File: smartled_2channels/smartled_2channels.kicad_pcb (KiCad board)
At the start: 2 copper layers, 76 parts, among them J1 Conn_01x04, J2 Conn_01x02, SW1 SW_Push, U1 OC5028B, U2 MAX485E, U3 PY32F003F1xUx, U4 OC5864, U5 SGM2033-3.3, U6 OC5028B, U7 GS8521

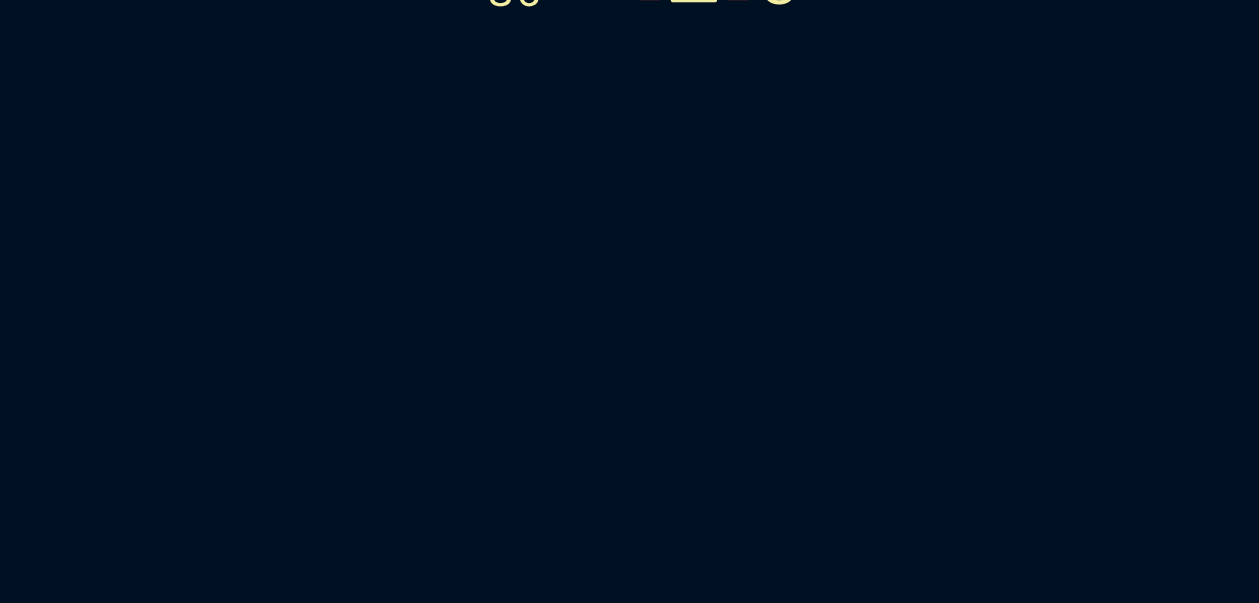
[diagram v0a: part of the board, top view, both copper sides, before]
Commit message: 添加麦克风声感应电路，红外和雷达传感器接口
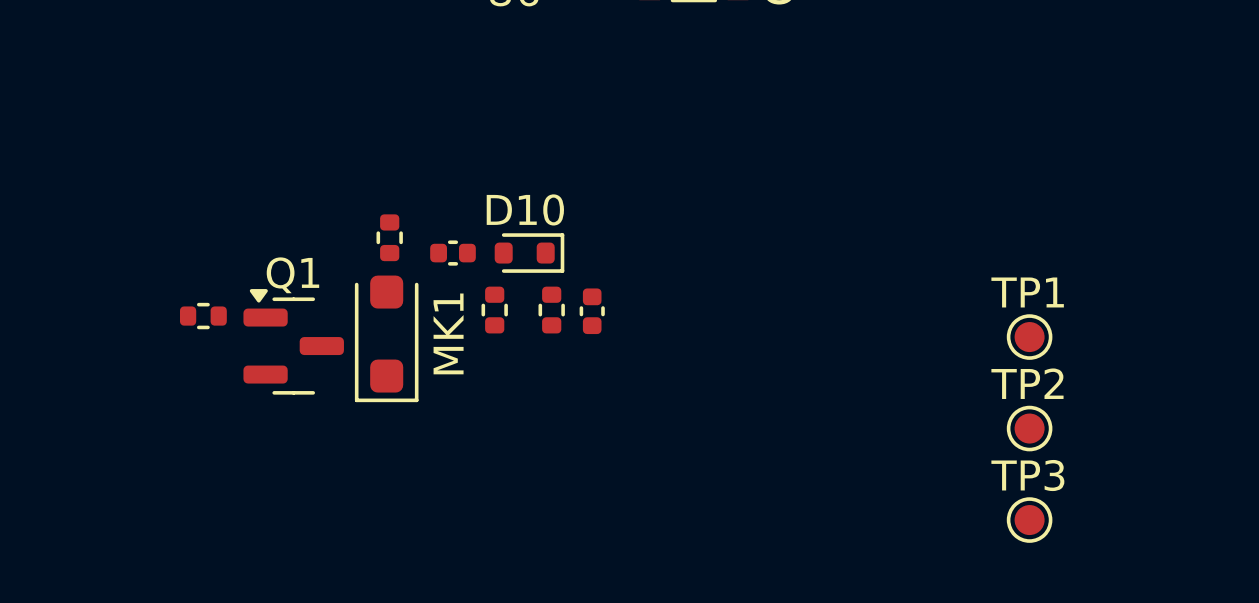
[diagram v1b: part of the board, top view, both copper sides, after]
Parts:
- added C10: 100n, Capacitor_SMD:C_0402_1005Metric, F.Cu at (157.7, 111.1)
- added C14: 100n, Capacitor_SMD:C_0402_1005Metric, F.Cu at (162.3, 113.0)
- added D10: D, Diode_SMD:D_SOD-523, F.Cu at (160.1, 111.1)
- added MK1: Microphone, Diode_SMD:D_SOD-123F, F.Cu at (155.5, 113.8)
- added Q1: Q_NMOS_GSD, Package_TO_SOT_SMD:SOT-23, F.Cu at (152.4, 114.2)
- added R21: 47k, Resistor_SMD:R_0402_1005Metric, F.Cu at (155.6, 110.6)
- added R22: 100k, Resistor_SMD:R_0402_1005Metric, F.Cu at (159.1, 113.0)
- added R24: 200k, Resistor_SMD:R_0402_1005Metric, F.Cu at (161.0, 113.0)
- added R25: 1k, Resistor_SMD:R_0402_1005Metric, F.Cu at (149.4, 113.2)
- added TP1: TestPoint, TestPoint:TestPoint_Pad_D1.0mm, F.Cu at (176.9, 113.9)
- added TP2: TestPoint, TestPoint:TestPoint_Pad_D1.0mm, F.Cu at (176.9, 117.0)
- added TP3: TestPoint, TestPoint:TestPoint_Pad_D1.0mm, F.Cu at (176.9, 120.0)
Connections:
- U3 pad 13: unconnected-(U3-OSCIN_PF0-Pad13) -> /INT_RADAR
- U3 pad 14: unconnected-(U3-OSCOUT_PF1-Pad14) -> /INT_IR
- U3 pad 15: unconnected-(U3-NRST_PF2-Pad15) -> /DET_EN
- U3 pad 17: /PWM4 -> /ADC_RADAR
- U3 pad 19: /PWM3 -> /ADC_MIC

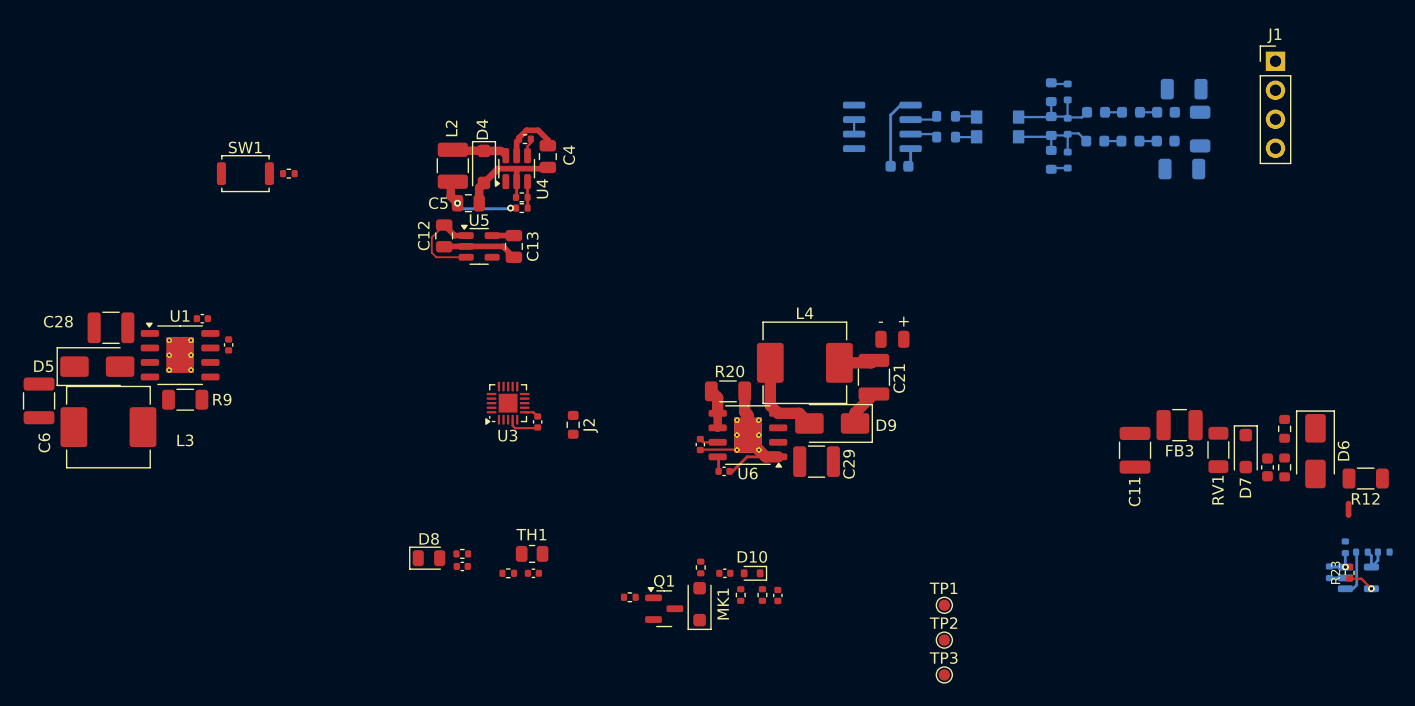
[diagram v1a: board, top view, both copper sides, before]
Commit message: 压缩布局至85.4x16mm尺寸
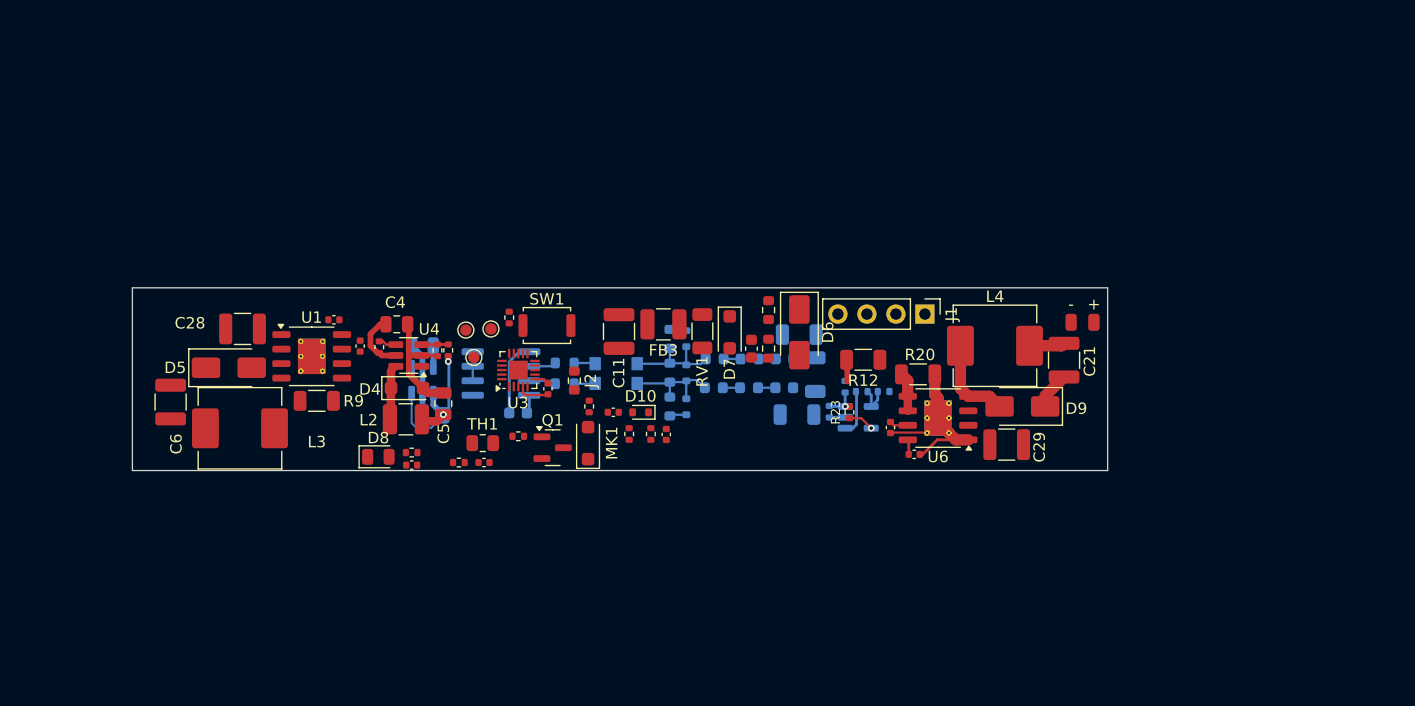
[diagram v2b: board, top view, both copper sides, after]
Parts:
- C12, C13, U5: moved to B.Cu
- moved TP3 51.6 mm to (135.0, 89.8), turned to 90 degrees
- moved TP2 48.2 mm to (137.2, 89.7), turned to 90 degrees
- moved TP1 46.6 mm to (135.7, 92.2), turned to 90 degrees
- moved C11 46.4 mm to (148.4, 89.9)
- moved C9 46.4 mm to (160.0, 91.4)
- moved D6 46.4 mm to (164.2, 90.0)
- moved D7 46.4 mm to (158.1, 90.0)
- moved R10 46.4 mm to (161.5, 88.0)
- moved R11 46.4 mm to (161.5, 91.4)
- moved RV1 46.4 mm to (155.7, 89.9)
- moved FB3 46.1 mm to (152.3, 89.3)
- moved R18 46.0 mm to (169.7, 95.2)
- moved R23 46.0 mm to (168.6, 97.0)
- moved R16 46.0 mm to (168.2, 94.8)
- moved R17 46.0 mm to (171.6, 95.2)
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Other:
- board outline added: 85.4 x 16 mm

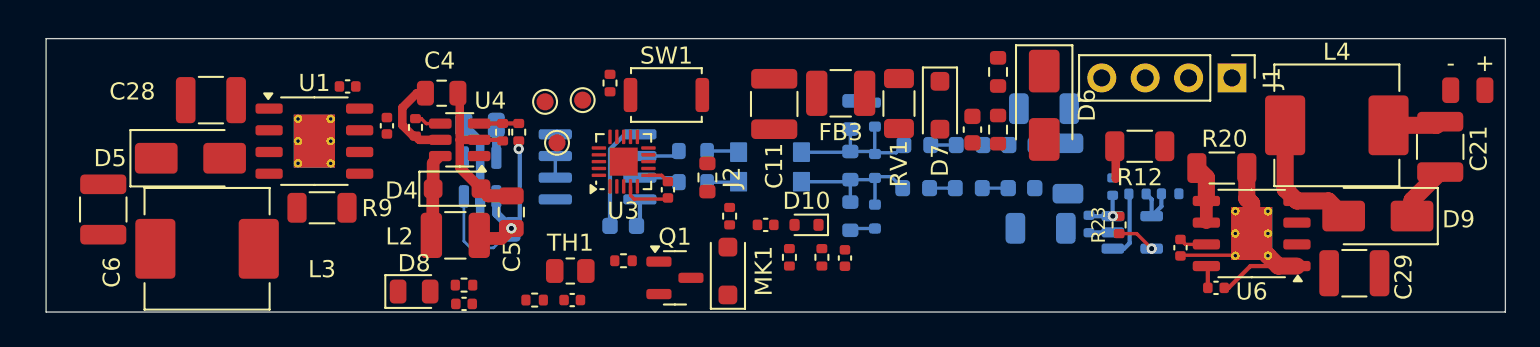
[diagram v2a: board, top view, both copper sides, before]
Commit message: 进行布线，微调原理图
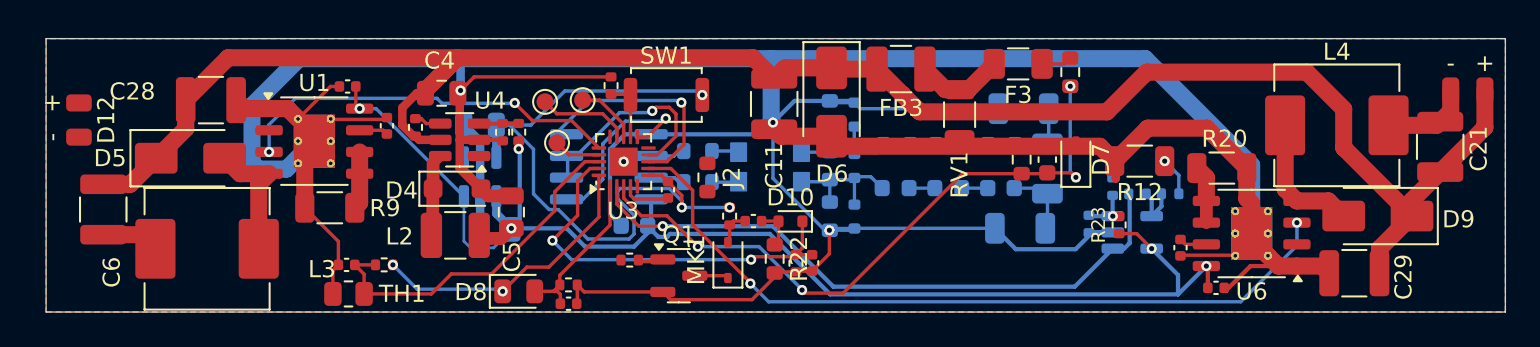
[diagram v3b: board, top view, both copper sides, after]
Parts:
- removed J1: Conn_01x04, Connector_PinHeader_2.54mm:PinHeader_1x04_P2.54mm_Vertical
- added D12: LED_Series, project_footprints:2Pads_1.0x1.5mm_P2.0mm_mpsign, F.Cu at (107.7, 90.9)
- added F3: Fuse, Fuse:Fuse_1206_3216Metric, F.Cu at (162.7, 87.6)
- D7, MK1: footprint Diode_SMD:D_SOD-123F -> Diode_SMD:D_SOD-323
- R22: footprint Resistor_SMD:R_0402_1005Metric -> Resistor_SMD:R_0603_1608Metric
- moved C17 13.4 mm to (123.4, 99.3), turned to 180 degrees
- moved TH1 13.0 mm to (123.5, 101.0), turned to 180 degrees
- moved D6 12.4 mm to (151.8, 89.8)
- moved R15 9.04 mm to (125.6, 99.3), turned to 180 degrees
- moved D7 8.56 mm to (166.1, 93.2), turned to 90 degrees
- moved C18 6.12 mm to (136.4, 101.6)
- moved D8 6.12 mm to (133.5, 100.9)
- moved R14 6.12 mm to (136.4, 100.5)
- moved C9 4.72 mm to (164.4, 93.2), turned to 90 degrees
- moved R10 4.23 mm to (165.7, 88.1)
- moved FB3 3.80 mm to (155.8, 87.9)
- moved RV1 3.61 mm to (159.3, 90.6)
- moved R11 2.23 mm to (162.9, 93.2), turned to 90 degrees
- moved C14 1.94 mm to (150.6, 99.2)
- moved R24 1.56 mm to (149.7, 99.2)
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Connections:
- R23 pad 1: +3.3V -> +5V
- U7 pad 5: +3.3V -> +5V
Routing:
- net GND: track 49.6 -> 258.4 mm, vias 0 -> 4
- net VINP: track 8.56 -> 109.7 mm
- net +5V: track 18.8 -> 78.2 mm, vias 2 -> 5
- net /PWM2: track 0.00 -> 45.1 mm, vias 0 -> 2
- net /ADC_V: track 0.00 -> 38.0 mm, vias 0 -> 4
- net +3.3V: track 5.47 -> 40.7 mm, vias 1 -> 3
- net /ADC_I: track 4.02 -> 37.0 mm, vias 0 -> 1
- net /ADC_MIC: track 0.00 -> 23.5 mm, vias 0 -> 2
- net /PWM1: track 0.00 -> 22.8 mm, vias 0 -> 2
- net /ADC_T: track 0.00 -> 20.7 mm
- net /SampEn: track 0.00 -> 16.9 mm, vias 0 -> 2
- net /MAX485_DI: track 0.00 -> 13.3 mm, vias 0 -> 1
- net /MAX485_RO: track 0.00 -> 11.7 mm, vias 0 -> 1
- net /MAX485_TR: track 1.27 -> 12.3 mm, vias 0 -> 1
- net /ADC_PD: track 0.00 -> 9.51 mm
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- added copper zone on B.Cu, net GND
- added copper zone on F.Cu, net GND

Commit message: 连接一些未连接项目
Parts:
- moved TP3 0.46 mm to (135.2, 89.4)
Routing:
- net /DET_EN: track 0.00 -> 15.5 mm, vias 0 -> 2
- net /ADC_MIC: track 23.5 -> 25.6 mm
- net GND: track 258.4 -> 260.0 mm, vias 4 -> 5
- net +5V: track 78.2 -> 78.9 mm
- net +3.3V: track 40.7 -> 41.3 mm

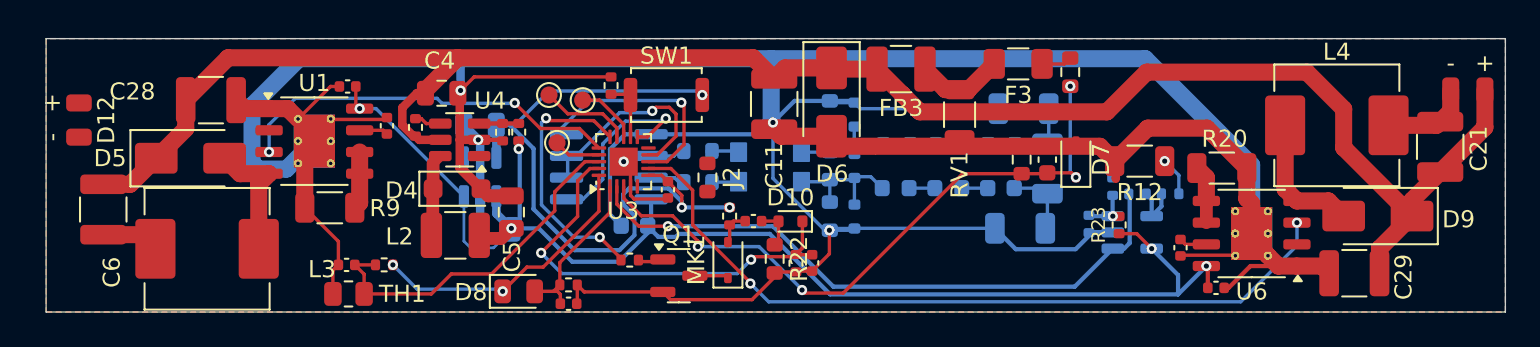
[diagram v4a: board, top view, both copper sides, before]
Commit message: 修改LED输出焊盘，缩短PCB长度到83mm
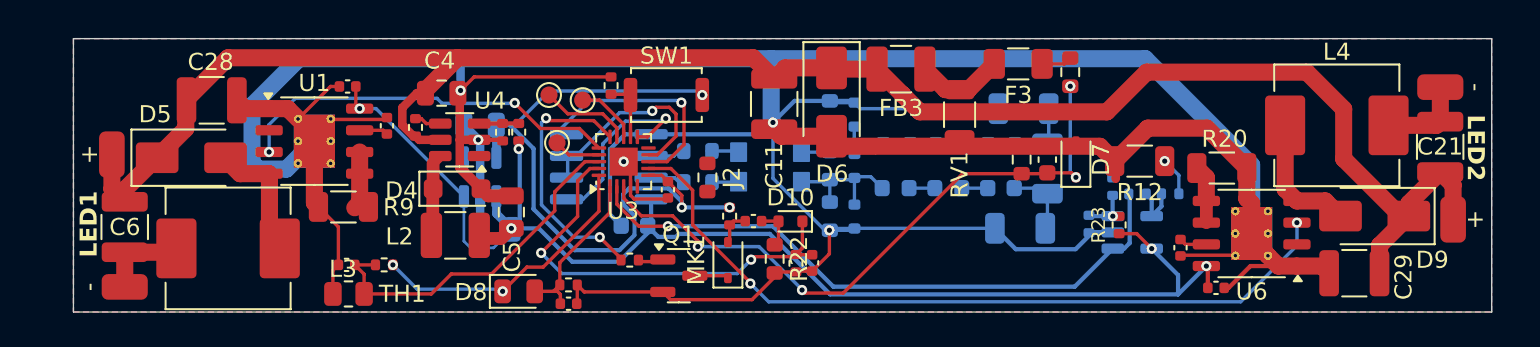
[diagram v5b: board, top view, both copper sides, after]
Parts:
- D12, D13: footprint project_footprints:2Pads_1.0x1.5mm_P2.0mm_mpsign -> project_footprints:2Pads_1.5x2.7mm_Tshape_mpsign
- moved D12 6.81 mm to (110.4, 97.1)
- moved D13 3.69 mm to (187.4, 92.4), turned to -90 degrees
- moved C6 1.62 mm to (110.4, 97.1)
- moved L3 1.23 mm to (116.5, 98.4)
- moved R9 0.80 mm to (123.2, 96.0)
- moved D9 0.19 mm to (183.6, 96.5)
- moved D5 0.06 mm to (114.3, 93.1)
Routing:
- net Net-(D12-K): track 3.39 -> 5.15 mm
- net GND: track 260.0 -> 259.5 mm
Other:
- board size 85.4 x 16 mm -> 83 x 16 mm
- board text added: "LED1"
- board text added: "LED2"

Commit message: 修改丝印
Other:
- board text added: "LED Strip 2 Channel Driver yyyy.mm.dd vx.x-gxxxxxxx Copyright (C) 2026 徐瑞骏 License under CERN-OHL-S v2"
- board text added: "https://github.com/XuHg-zjcn/smartled_controll"
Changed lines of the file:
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@@
 		(tags "Diode SOD523")
 		(property "Reference" "D10"
-			(at 0 1.4 0)
+			(at -2.8496 -0.0058 0)
 			(layer "F.SilkS")
 			(effects
@@
 		(tags "resistor")
 		(property "Reference" "R9"
-			(at -3.2325 -0.025 0)
+			(at -0.33 -1.77 0)
 			(layer "F.SilkS")
 			(effects
@@
 		(tags "SOD-323")
 		(property "Reference" "MK1"
-			(at 0 -1.85 90)
+			(at -2.4 0.71 180)
 			(layer "F.SilkS")
 			(effects
@@
 		(tags "SOD-323")
 		(property "Reference" "D7"
-			(at 0 1.4732 90)
+			(at 1.9272 0.0548 180)
 			(layer "F.SilkS")
 			(effects
@@
 		(tags "resistor")
 		(property "Reference" "R22"
-			(at 0 -1.43 -90)
+			(at 2.2298 0.0076 0)
 			(layer "F.SilkS")
+			(hide yes)
 			(effects
 				(font
@@
 		(tags "Inductor molded power shielded")
 		(property "Reference" "L3"
-			(at -6.725 -1.2 0)
+			(at -4.87 -0.135 -90)
 			(layer "F.SilkS")
 			(effects
@@
 		(tags "capacitor")
 		(property "Reference" "C2"
-			(at -0.005 1.34 0)
+			(at -2.05 2.55 0)
 			(layer "B.SilkS")
 			(effects
@@
 		(tags "capacitor")
 		(property "Reference" "C1"
-			(at 0.075 -1.4 0)
+			(at -1.96 -2.83 0)
 			(layer "B.SilkS")
 			(effects
@@
 			(at -0.01 1.26 90)
 			(layer "B.SilkS")
+			(hide yes)
 			(effects
 				(font
@@
 		(layer "Edge.Cuts")
 	)
+	(gr_text "https://github.com/XuHg-zjcn/smartled_controll"
+		(at 139.49 100.9 0)
+		(layer "B.SilkS")
+		(effects
+			(font
+				(size 0.8 0.8)
+				(thickness 0.1)
+			)
+			(justify left bottom mirror)
+		)
+	)
+	(gr_text "LED Strip 2 Channel Driver\nyyyy.mm.dd vx.x-gxxxxxxx\n\nCopyright (C) 2026  徐瑞骏\nLicense under CERN-OHL-S v2"
+		(at 128.54 97.11 0)
+		(layer "B.SilkS")
+		(effects
+			(font
+				(size 0.8 0.8)
+				(thickness 0.1)
+			)
+			(justify left bottom mirror)
+		)
+	)
 	(gr_text "LED1"
 		(at 108.88 98.91 90)
@@
 	)
 	(segment
-		(start 124.15 95.7125)
-		(end 123.8625 96)
+		(start 124.15 95.4375)
+		(end 124.6625 95.95)
 		(width 1)
 		(layer "F.Cu")
@@
 	(segment
 		(start 124.15 92.735)
-		(end 124.15 95.7125)
+		(end 124.15 95.4375)
 		(width 1)
 		(layer "F.Cu")
@@
 	)
 	(group "LED驱动1"
-		(members "097316fb-18b5-480e-862f-6f3a3067adb6" "178e6880-8828-4553-bee4-e2de0b5de154"
-			"17a861f3-fc8d-4d16-9c42-8d2c828430de" "1b08897a-7ea3-4d59-91b4-9b10cab0b1a9"
-			"2033e229-ce9b-4350-acb4-26b53c010734" "20926de3-6061-49c6-a51c-7a7e43ec4d50"
-			"2152c6b9-174d-424b-a63c-def9bc6348bc" "2a837293-223a-42a8-b839-e46fae8bb605"
-			"2c3bac7e-ebed-4ce1-8919-bbaeaaef3147" "2dabf7f8-eef8-4994-8a27-e8a169fa6792"
-			"2e25fb8c-2a1e-4550-b22c-549ad53cfbc1" "32ae1743-d038-41f1-94bd-7f9fbec4ed90"
-			"37747a8a-c22f-403b-aec3-d528845dcaa8" "479d0d2b-0dce-436a-b1ad-8536b169c966"
-			"48e1d37f-9f97-467d-ba60-32f792c0eb09" "4bd7aa62-10d7-493a-9aaa-15b3a4a61b62"
-			"4c631bd3-adb7-4b47-ab74-286c30ad1970" "50ea2e16-1790-43fd-bae8-e2b482237c03"
+		(members "097316fb-18b5-480e-862f-6f3a3067adb6" "148c36cd-57e3-43ec-9491-cfc7f3f19676"
+			"178e6880-8828-4553-bee4-e2de0b5de154" "17a861f3-fc8d-4d16-9c42-8d2c828430de"
+			"1b08897a-7ea3-4d59-91b4-9b10cab0b1a9" "2033e229-ce9b-4350-acb4-26b53c010734"
+			"20926de3-6061-49c6-a51c-7a7e43ec4d50" "2152c6b9-174d-424b-a63c-def9bc6348bc"
+			"2a837293-223a-42a8-b839-e46fae8bb605" "2c3bac7e-ebed-4ce1-8919-bbaeaaef3147"
+			"2dabf7f8-eef8-4994-8a27-e8a169fa6792" "2e25fb8c-2a1e-4550-b22c-549ad53cfbc1"
+			"32ae1743-d038-41f1-94bd-7f9fbec4ed90" "37747a8a-c22f-403b-aec3-d528845dcaa8"
+			"479d0d2b-0dce-436a-b1ad-8536b169c966" "48e1d37f-9f97-467d-ba60-32f792c0eb09"
+			"4bd7aa62-10d7-493a-9aaa-15b3a4a61b62" "50ea2e16-1790-43fd-bae8-e2b482237c03"
 			"5f62f44f-4703-41c8-b04c-5f74c7fc2fa3" "64d6868a-f9e5-42c9-b998-cb720dfef56b"
 			"65e27c9f-d16f-4031-9ffd-fc2fd826a6a9" "753afaa1-0ebb-4073-b54f-fe7017cab049"
-			"885f5cca-6205-41b3-8391-836988e3b475" "8bb596f6-43d5-4901-afc0-677bb19a7014"
-			"92ab89e0-2686-4027-b9c7-53db87f32243" "9ab00480-09d2-4213-bb03-b5a6c376febe"
-			"9ed58afb-b925-41c1-a761-3c7b812ba96b" "a7faf8e1-2291-459a-92ee-ab987d4345db"
-			"b2a820eb-b783-4e1f-b83a-a7a0dae965ab" "b6b19472-3ec6-4e39-a0d9-930934425199"
-			"c131a8dc-823a-4ff3-ac65-e482af8cea7b" "c5b485b0-9534-4048-8b82-fd68a3d97f9b"
-			"c7fab91c-4a26-4925-a85d-e27f202add17" "c9de9c0f-0f86-485d-95b1-522b2afedfa7"
-			"cbaaa079-b1ac-4352-920c-a6d986f916e2" "cf28c322-ef8d-43d5-b11a-afce221be219"
-			"d046ca46-3bda-4053-bcc6-fac1c8a76122" "d375a6a1-f7a1-4595-9121-b7cf7fc391a4"
-			"dfee9b27-3236-48ec-b161-496387d06598" "e252ca6d-3f8a-428d-9d2a-bdb01b820655"
-			"ea9a6746-549a-4075-92a4-326294cc27fc" "ecc175c0-710b-4301-a438-8fe1630de94f"
-			"f754da91-fb3b-4141-b952-57b58db5bc32"
+			"885f5cca-6205-41b3-8391-836988e3b475" "92ab89e0-2686-4027-b9c7-53db87f32243"
+			"9ab00480-09d2-4213-bb03-b5a6c376febe" "9ed58afb-b925-41c1-a761-3c7b812ba96b"
+			"a7faf8e1-2291-459a-92ee-ab987d4345db" "b2a820eb-b783-4e1f-b83a-a7a0dae965ab"
+			"b6b19472-3ec6-4e39-a0d9-930934425199" "c131a8dc-823a-4ff3-ac65-e482af8cea7b"
+			"c5b485b0-9534-4048-8b82-fd68a3d97f9b" "c7fab91c-4a26-4925-a85d-e27f202add17"
+			"c9de9c0f-0f86-485d-95b1-522b2afedfa7" "cbaaa079-b1ac-4352-920c-a6d986f916e2"
+			"cf28c322-ef8d-43d5-b11a-afce221be219" "d046ca46-3bda-4053-bcc6-fac1c8a76122"
+			"d375a6a1-f7a1-4595-9121-b7cf7fc391a4" "dfee9b27-3236-48ec-b161-496387d06598"
+			"e252ca6d-3f8a-428d-9d2a-bdb01b820655" "ea9a6746-549a-4075-92a4-326294cc27fc"
+			"ecc175c0-710b-4301-a438-8fe1630de94f" "f754da91-fb3b-4141-b952-57b58db5bc32"
+			"fe8cd0fd-9be1-4f2d-8946-2528d3ad1bf7"
 		)
 	)
